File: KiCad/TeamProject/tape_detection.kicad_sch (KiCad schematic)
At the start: 5 parts, among them U10 Tape Sensor, U11 Tape Sensor, U3 Tape Sensor, U8 Tape Sensor, U9 Tape Sensor

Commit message: Kicad Update
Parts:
- removed U10, U11: Tape Sensor, symbol ME218_BaseLib:SW_CapTouch
- renumbered U9 to U, U3 to U, U8 to U

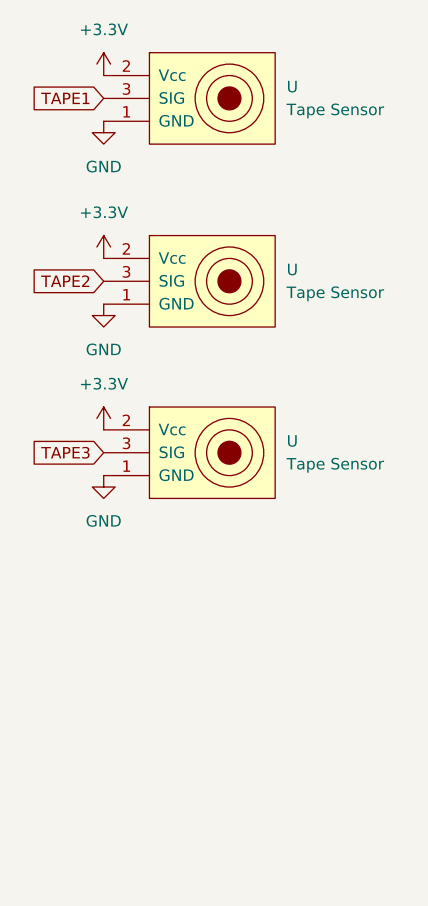
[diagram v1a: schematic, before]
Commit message: change Pin of SPI
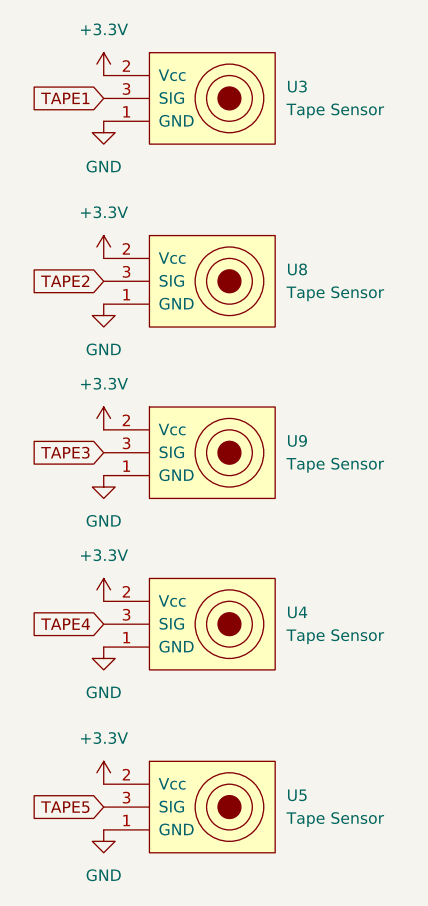
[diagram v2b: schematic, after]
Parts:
- added U4, U5: Tape Sensor, symbol ME218_BaseLib:SW_CapTouch
- renumbered U to U3, U to U8, U to U9
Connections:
- net +3.3V: now also U4.2 (Vcc), U5.2 (Vcc)
- net GND: now also U4.1 (GND), U5.1 (GND)
- new net TAPE4: U4.3 (SIG)
- new net TAPE5: U5.3 (SIG)
